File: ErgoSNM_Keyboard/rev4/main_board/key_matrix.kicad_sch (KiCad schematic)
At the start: 69 parts

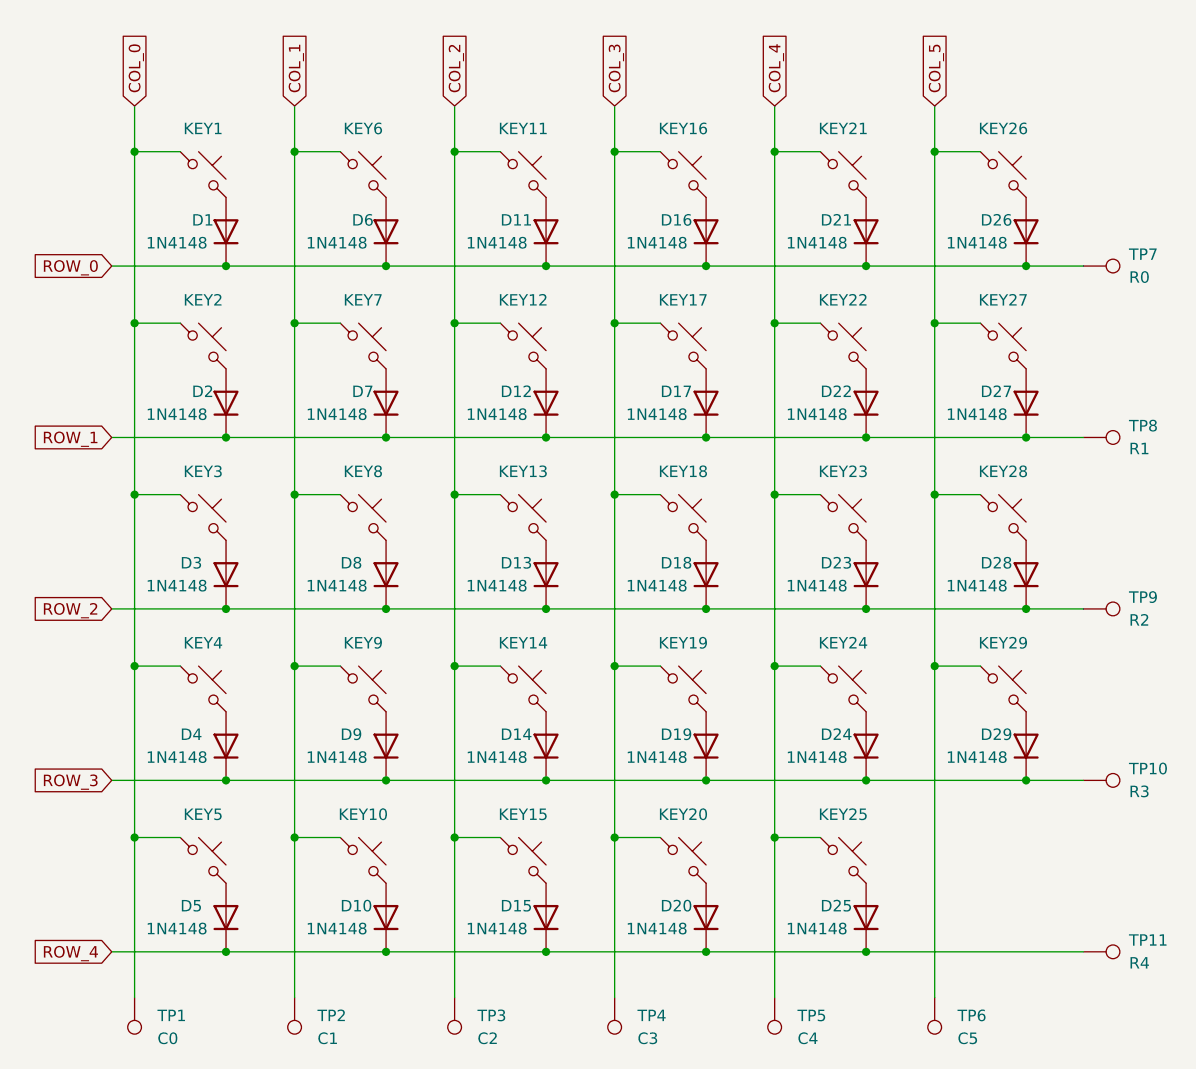
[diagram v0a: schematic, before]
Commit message: feat: add v4 mdbt50q board
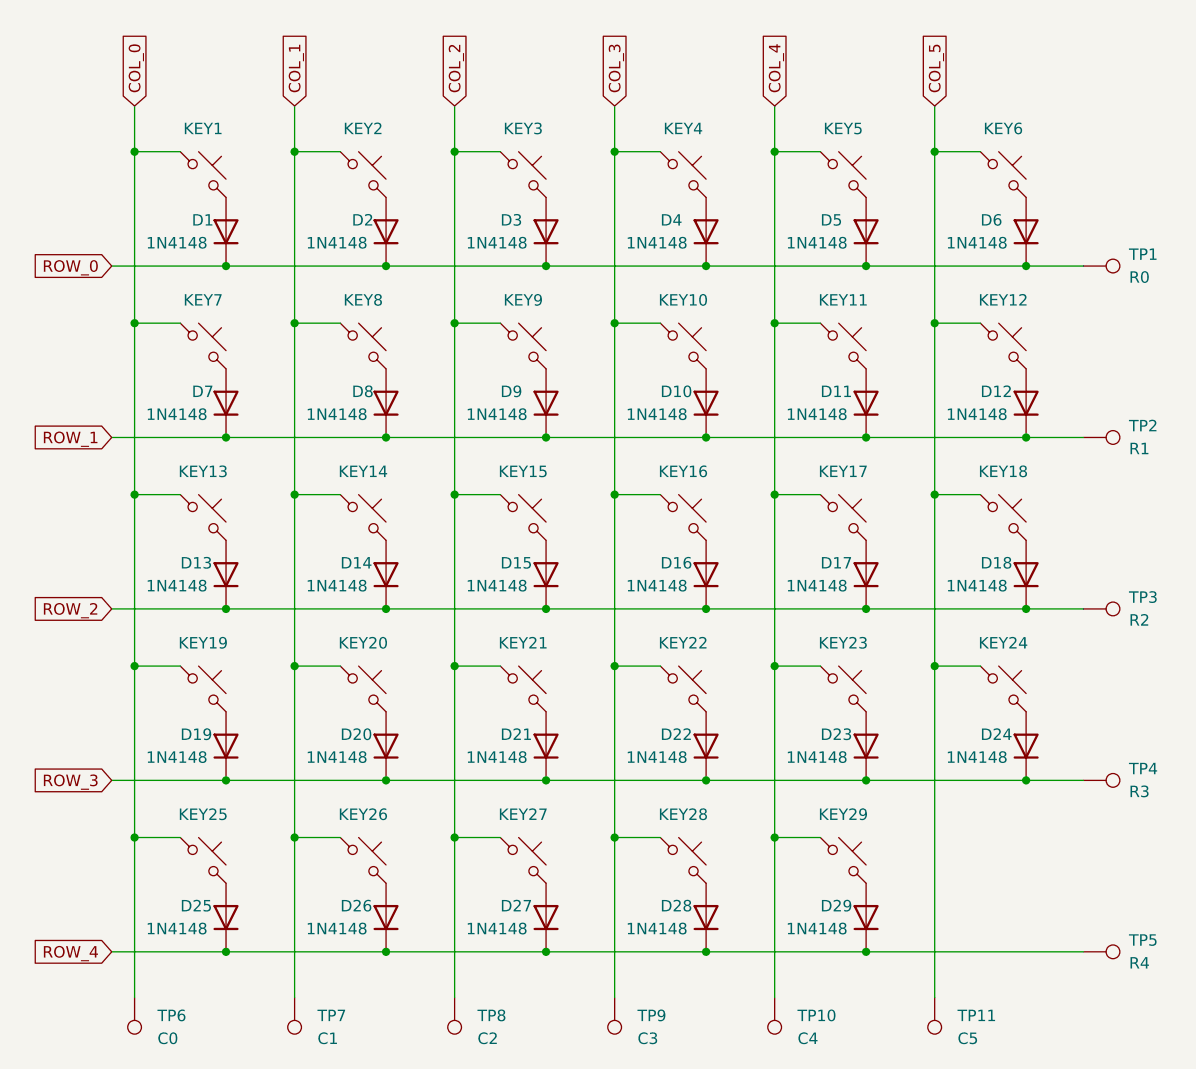
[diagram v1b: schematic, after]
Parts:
- KEY1: footprint key-switches:SW_MX_Kailh_Choc_V1V2_HotSwap_Hybrid -> key-switches:SW_MX_Kailh_Choc_V1V2_HotSwap_Hybrid_double
- KEY10: renamed from KEY17; footprint key-switches:SW_MX_Kailh_Choc_V1V2_HotSwap_Hybrid -> key-switches:SW_MX_Kailh_Choc_V1V2_HotSwap_Hybrid_double
- KEY11: renamed from KEY22; footprint key-switches:SW_MX_Kailh_Choc_V1V2_HotSwap_Hybrid -> key-switches:SW_MX_Kailh_Choc_V1V2_HotSwap_Hybrid_double
- KEY12: renamed from KEY27; footprint key-switches:SW_MX_Kailh_Choc_V1V2_HotSwap_Hybrid -> key-switches:SW_MX_Kailh_Choc_V1V2_HotSwap_Hybrid_double
- KEY13: renamed from KEY3; footprint key-switches:SW_MX_Kailh_Choc_V1V2_HotSwap_Hybrid -> key-switches:SW_MX_Kailh_Choc_V1V2_HotSwap_Hybrid_double
- KEY14: renamed from KEY8; footprint key-switches:SW_MX_Kailh_Choc_V1V2_HotSwap_Hybrid -> key-switches:SW_MX_Kailh_Choc_V1V2_HotSwap_Hybrid_double
- KEY15: renamed from KEY13; footprint key-switches:SW_MX_Kailh_Choc_V1V2_HotSwap_Hybrid -> key-switches:SW_MX_Kailh_Choc_V1V2_HotSwap_Hybrid_double
- KEY16: renamed from KEY18; footprint key-switches:SW_MX_Kailh_Choc_V1V2_HotSwap_Hybrid -> key-switches:SW_MX_Kailh_Choc_V1V2_HotSwap_Hybrid_double
- KEY17: renamed from KEY23; footprint key-switches:SW_MX_Kailh_Choc_V1V2_HotSwap_Hybrid -> key-switches:SW_MX_Kailh_Choc_V1V2_HotSwap_Hybrid_double
- KEY18: renamed from KEY28; footprint key-switches:SW_MX_Kailh_Choc_V1V2_HotSwap_Hybrid -> key-switches:SW_MX_Kailh_Choc_V1V2_HotSwap_Hybrid_double
- KEY19: renamed from KEY4; footprint key-switches:SW_MX_Kailh_Choc_V1V2_HotSwap_Hybrid -> key-switches:SW_MX_Kailh_Choc_V1V2_HotSwap_Hybrid_double
- KEY2: renamed from KEY6; footprint key-switches:SW_MX_Kailh_Choc_V1V2_HotSwap_Hybrid -> key-switches:SW_MX_Kailh_Choc_V1V2_HotSwap_Hybrid_double
- KEY20: renamed from KEY9; footprint key-switches:SW_MX_Kailh_Choc_V1V2_HotSwap_Hybrid -> key-switches:SW_MX_Kailh_Choc_V1V2_HotSwap_Hybrid_double
- KEY21: renamed from KEY14; footprint key-switches:SW_MX_Kailh_Choc_V1V2_HotSwap_Hybrid -> key-switches:SW_MX_Kailh_Choc_V1V2_HotSwap_Hybrid_double
- KEY22: renamed from KEY19; footprint key-switches:SW_MX_Kailh_Choc_V1V2_HotSwap_Hybrid -> key-switches:SW_MX_Kailh_Choc_V1V2_HotSwap_Hybrid_double
- KEY23: renamed from KEY24; footprint key-switches:SW_MX_Kailh_Choc_V1V2_HotSwap_Hybrid -> key-switches:SW_MX_Kailh_Choc_V1V2_HotSwap_Hybrid_double
- KEY24: renamed from KEY29; footprint key-switches:SW_MX_Kailh_Choc_V1V2_HotSwap_Hybrid -> key-switches:SW_MX_Kailh_Choc_V1V2_HotSwap_Hybrid_double
- KEY25: renamed from KEY5; footprint key-switches:SW_MX_Kailh_Choc_V1V2_HotSwap_Hybrid -> key-switches:SW_MX_Kailh_Choc_V1V2_HotSwap_Hybrid_double
- KEY26: renamed from KEY10; footprint key-switches:SW_MX_Kailh_Choc_V1V2_HotSwap_Hybrid -> key-switches:SW_MX_Kailh_Choc_V1V2_HotSwap_Hybrid_double
- KEY27: renamed from KEY15; footprint key-switches:SW_MX_Kailh_Choc_V1V2_HotSwap_Hybrid -> key-switches:SW_MX_Kailh_Choc_V1V2_HotSwap_Hybrid_double
- KEY28: renamed from KEY20; footprint key-switches:SW_MX_Kailh_Choc_V1V2_HotSwap_Hybrid -> key-switches:SW_MX_Kailh_Choc_V1V2_HotSwap_Hybrid_double
- KEY29: renamed from KEY25; footprint key-switches:SW_MX_Kailh_Choc_V1V2_HotSwap_Hybrid -> key-switches:SW_MX_Kailh_Choc_V1V2_HotSwap_Hybrid_double
- KEY3: renamed from KEY11; footprint key-switches:SW_MX_Kailh_Choc_V1V2_HotSwap_Hybrid -> key-switches:SW_MX_Kailh_Choc_V1V2_HotSwap_Hybrid_double
- KEY4: renamed from KEY16; footprint key-switches:SW_MX_Kailh_Choc_V1V2_HotSwap_Hybrid -> key-switches:SW_MX_Kailh_Choc_V1V2_HotSwap_Hybrid_double
- KEY5: renamed from KEY21; footprint key-switches:SW_MX_Kailh_Choc_V1V2_HotSwap_Hybrid -> key-switches:SW_MX_Kailh_Choc_V1V2_HotSwap_Hybrid_double
- KEY6: renamed from KEY26; footprint key-switches:SW_MX_Kailh_Choc_V1V2_HotSwap_Hybrid -> key-switches:SW_MX_Kailh_Choc_V1V2_HotSwap_Hybrid_double
- KEY7: renamed from KEY2; footprint key-switches:SW_MX_Kailh_Choc_V1V2_HotSwap_Hybrid -> key-switches:SW_MX_Kailh_Choc_V1V2_HotSwap_Hybrid_double
- KEY8: renamed from KEY7; footprint key-switches:SW_MX_Kailh_Choc_V1V2_HotSwap_Hybrid -> key-switches:SW_MX_Kailh_Choc_V1V2_HotSwap_Hybrid_double
- KEY9: renamed from KEY12; footprint key-switches:SW_MX_Kailh_Choc_V1V2_HotSwap_Hybrid -> key-switches:SW_MX_Kailh_Choc_V1V2_HotSwap_Hybrid_double
- renumbered D17 to D10, D22 to D11, D27 to D12, D3 to D13, D8 to D14, D13 to D15, D18 to D16, D23 to D17, D28 to D18, D4 to D19, D6 to D2, D9 to D20, D14 to D21, D19 to D22, D24 to D23, D29 to D24, D5 to D25, D10 to D26, D15 to D27, D20 to D28, D25 to D29, D11 to D3, D16 to D4, D21 to D5, D26 to D6, D2 to D7, D7 to D8, D12 to D9, TP7 to TP1, TP5 to TP10, TP6 to TP11, TP8 to TP2, TP9 to TP3, TP10 to TP4, TP11 to TP5, TP1 to TP6, TP2 to TP7, TP3 to TP8, TP4 to TP9

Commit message: feat: update the connectors of the main board and core board
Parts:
- KEY1, KEY10, KEY11, KEY12, KEY13, KEY14, KEY15, KEY16, KEY17, KEY18, KEY19, KEY2, KEY20, KEY21, KEY22, KEY23, KEY24, KEY25, KEY26, KEY27, KEY28, KEY29, KEY3, KEY4, KEY5, KEY6, KEY7, KEY8, KEY9: now left out of the parts list
